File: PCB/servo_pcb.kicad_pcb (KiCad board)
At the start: 2 copper layers, 32.5 x 23 mm, 26 parts, among them M1 M1, M2 M2, M3 VCC, M4 GND, M5 DATA, U1 MM32G0001, U2 SL7533-3, U3 CP2119L, U4 INA180A2

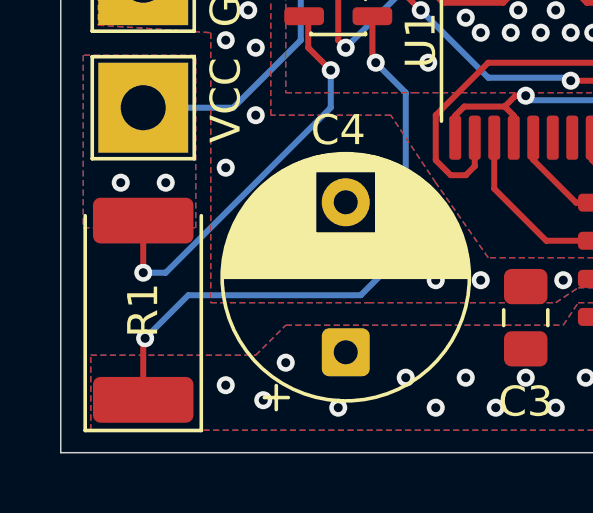
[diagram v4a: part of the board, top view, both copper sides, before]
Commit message: docs: added OSHWA certification, contributing guide, and issue templates
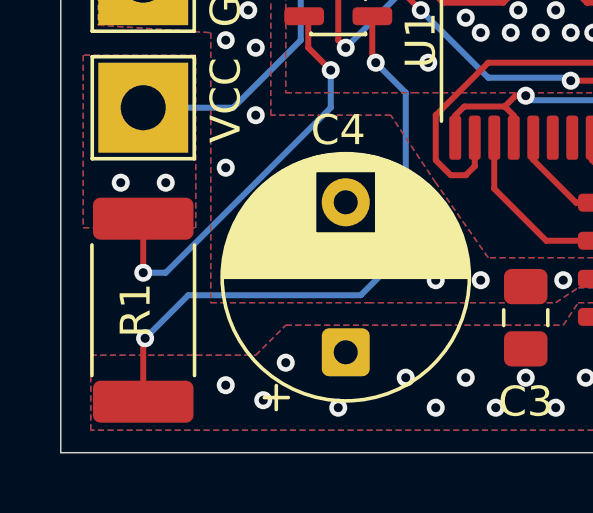
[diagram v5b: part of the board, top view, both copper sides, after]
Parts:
- R1: footprint Diode_SMD:D_2512_6332Metric_Pad1.52x3.35mm_HandSolder -> Resistor_SMD:R_2512_6332Metric_Pad1.40x3.35mm_HandSolder
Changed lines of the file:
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@@
 	(generator_version "9.0")
 	(general
-		(thickness 1.6)
+		(thickness 1.69)
 		(legacy_teardrops no)
 	)
@@
 			(layer "F.SilkS"
 				(type "Top Silk Screen")
+				(color "White")
 			)
 			(layer "F.Paste"
@@
 			(layer "F.Mask"
 				(type "Top Solder Mask")
+				(color "Purple")
 				(thickness 0.01)
 			)
@@
 			(layer "dielectric 1"
 				(type "core")
-				(thickness 1.51)
+				(color "FR4 natural")
+				(thickness 1.6)
 				(material "FR4")
 				(epsilon_r 4.5)
@@
 			(layer "B.Mask"
 				(type "Bottom Solder Mask")
+				(color "Purple")
 				(thickness 0.01)
 			)
@@
 			(layer "B.SilkS"
 				(type "Bottom Silk Screen")
-			)
-			(copper_finish "None")
+				(color "White")
+			)
+			(copper_finish "HAL SnPb")
 			(dielectric_constraints no)
 		)
@@
 		)
 	)
-	(footprint "Diode_SMD:D_2512_6332Metric_Pad1.52x3.35mm_HandSolder"
+	(footprint "Resistor_SMD:R_2512_6332Metric_Pad1.40x3.35mm_HandSolder"
 		(layer "F.Cu")
 		(at 117.25 54.75 90)
-		(descr "Diode SMD 2512 (6332 Metric), square (rectangular) end terminal, IPC-7351 nominal, (Body size source: http://www.tortai-tech.com/upload/download/2011102023233369053.pdf), generated with kicad-footprint-generator")
-		(tags "diode handsolder")
+		(descr "Resistor SMD 2512 (6332 Metric), square (rectangular) end terminal, IPC-7351 nominal with elongated pad for handsoldering. (Body size source: IPC-SM-782 page 72, https://www.pcb-3d.com/wordpress/wp-content/uploads/ipc-sm-782a_amendment_1_and_2.pdf), generated with kicad-footprint-generator")
+		(tags "resistor handsolder")
 		(property "Reference" "R1"
-			(at 0 0 90)
+			(at 0 -0.25 90)
 			(layer "F.SilkS")
 			(effects
@@
 			)
 		)
-		(property "Datasheet" "~"
+		(property "Datasheet" ""
 			(at 0 0 90)
 			(layer "F.Fab")
@@
 			)
 		)
-		(property "Description" "Resistor"
+		(property "Description" ""
 			(at 0 0 90)
 			(layer "F.Fab")
@@
 		(attr smd)
 		(fp_line
-			(start 3.15 -1.935)
-			(end -4.01 -1.935)
-			(stroke
-				(width 0.12)
-				(type solid)
-			)
-			(layer "F.SilkS")
-		)
-		(fp_line
-			(start -4.01 -1.935)
-			(end -4.01 1.935)
-			(stroke
-				(width 0.12)
-				(type solid)
-			)
-			(layer "F.SilkS")
-		)
-		(fp_line
-			(start -4.01 1.935)
-			(end 3.15 1.935)
+			(start -2.177064 -1.71)
+			(end 2.177064 -1.71)
+			(stroke
+				(width 0.12)
+				(type solid)
+			)
+			(layer "F.SilkS")
+		)
+		(fp_line
+			(start -2.177064 1.71)
+			(end 2.177064 1.71)
 			(stroke
 				(width 0.12)
@@
 		(fp_line
 			(start 3.15 -1.6)
-			(end -2.35 -1.6)
-			(stroke
-				(width 0.1)
-				(type solid)
-			)
-			(layer "F.Fab")
-		)
-		(fp_line
-			(start -2.35 -1.6)
-			(end -3.15 -0.8)
-			(stroke
-				(width 0.1)
-				(type solid)
-			)
-			(layer "F.Fab")
-		)
-		(fp_line
-			(start -3.15 -0.8)
+			(end 3.15 1.6)
+			(stroke
+				(width 0.1)
+				(type solid)
+			)
+			(layer "F.Fab")
+		)
+		(fp_line
+			(start -3.15 -1.6)
+			(end 3.15 -1.6)
+			(stroke
+				(width 0.1)
+				(type solid)
+			)
+			(layer "F.Fab")
+		)
+		(fp_line
+			(start 3.15 1.6)
 			(end -3.15 1.6)
 			(stroke
@@
 		)
 		(fp_line
-			(start 3.15 1.6)
-			(end 3.15 -1.6)
-			(stroke
-				(width 0.1)
-				(type solid)
-			)
-			(layer "F.Fab")
-		)
-		(fp_line
 			(start -3.15 1.6)
-			(end 3.15 1.6)
+			(end -3.15 -1.6)
 			(stroke
 				(width 0.1)
@@
 		)
 		(pad "1" smd roundrect
-			(at -2.9875 0 90)
-			(size 1.525 3.35)
-			(layers "F.Cu" "F.Mask" "F.Paste")
-			(roundrect_rratio 0.163934)
+			(at -3.05 0 90)
+			(size 1.4 3.35)
+			(layers "F.Cu" "F.Mask" "F.Paste")
+			(roundrect_rratio 0.178571)
 			(net 5 "/DRIVER VCC")
 			(pintype "passive")
 		)
 		(pad "2" smd roundrect
-			(at 2.9875 0 90)
-			(size 1.525 3.35)
-			(layers "F.Cu" "F.Mask" "F.Paste")
-			(roundrect_rratio 0.163934)
+			(at 3.05 0 90)
+			(size 1.4 3.35)
+			(layers "F.Cu" "F.Mask" "F.Paste")
+			(roundrect_rratio 0.178571)
 			(net 4 "VCC")
 			(pintype "passive")
 		)
 		(embedded_fonts no)
-		(model "${KICAD9_3DMODEL_DIR}/Diode_SMD.3dshapes/D_2512_6332Metric.step"
+		(model "${KICAD9_3DMODEL_DIR}/Resistor_SMD.3dshapes/R_2512_6332Metric.step"
 			(offset
 				(xyz 0 0 0)
